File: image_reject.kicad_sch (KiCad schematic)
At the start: 21 parts, among them U1 MXD8546F, U9 MXD8638C

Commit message: Improve power supply filtering and decoupling
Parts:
- C10: value 1uF -> 1 uF
- C31: Substitution (none) -> GRM033R61A105ME44*, GRM033R61C105ME15*, Samsung CL03A105MO3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
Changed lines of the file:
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@@
 			)
 		)
-		(property "Value" "1uF"
+		(property "Value" "1 uF"
 			(at 143.51 171.4499 0)
 			(effects
@@
 			)
 		)
-		(property "Description" ""
+		(property "Description" "CAP CER 1UF 10V X5R 0201"
 			(at 151.13 170.18 0)
 			(effects
@@
 			(at 151.13 170.18 0)
 			(effects
+				(font
+					(size 1.27 1.27)
+				)
+				(hide yes)
+			)
+		)
+		(property "Substitution" "GRM033R61A105ME44*, GRM033R61C105ME15*, Samsung CL03A105MO3NRN*"
+			(at 151.13 170.18 0)
+			(effects

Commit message: Change SP3T RF switches from MXD8638C to BGS13SN8
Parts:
- U9: value MXD8638C -> BGS13SN8; symbol praline:MXD8638 -> praline:BGS13SN8; Manufacturer Maxscend -> Infineon; Part Number MXD8638C -> BGS13SN8E6327XTSA1
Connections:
- net 2V5RF: now also U9.1 (VDD); no longer U9.7 (VDD)
- net GND: now also U9.8 (GND); no longer U9.6 (GND)
- net LPF_OR_MIX_BYPASS: now also U9.2 (V2); no longer U9.8 (V2)
- net MIX_BYPASS: now also U9.7 (RF2); no longer U9.5 (RF2)
- net MIX_EN: now also U9.3 (V1); no longer U9.1 (V1)
- net RF: now also U9.6 (RFin); no longer U9.4 (ANT)
- net at C61.1, L15.1: now also U9.4 (RF3); no longer U9.2 (RF3)
- net at C96.2: now also U9.5 (RF1); no longer U9.3 (RF1)
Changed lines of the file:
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@@
 	)
 	(symbol
-		(lib_id "praline:MXD8638")
+		(lib_id "praline:BGS13SN8")
 		(at 224.79 69.85 0)
 		(unit 1)
@@
 			)
 		)
-		(property "Value" "MXD8638C"
+		(property "Value" "BGS13SN8"
 			(at 204.47 67.31 0)
 			(effects
@@
 			)
 		)
-		(property "Datasheet" "https://www.lcsc.com/datasheet/lcsc_datasheet_1912301210_Maxscend-MXD8638C_C285557.pdf"
+		(property "Datasheet" "https://www.infineon.com/dgdl/Infineon-BGS13SN8-DS-v02_02-EN.pdf?fileId=5546d462584d1d4a0158cf52e3ae03a7"
 			(at 224.79 69.85 0)
 			(effects
@@
 			)
 		)
-		(property "Manufacturer" "Maxscend"
+		(property "Manufacturer" "Infineon"
 			(at 224.79 69.85 0)
 			(effects
@@
 			)
 		)
-		(property "Part Number" "MXD8638C"
+		(property "Part Number" "BGS13SN8E6327XTSA1"
 			(at 224.79 69.85 0)
 			(effects

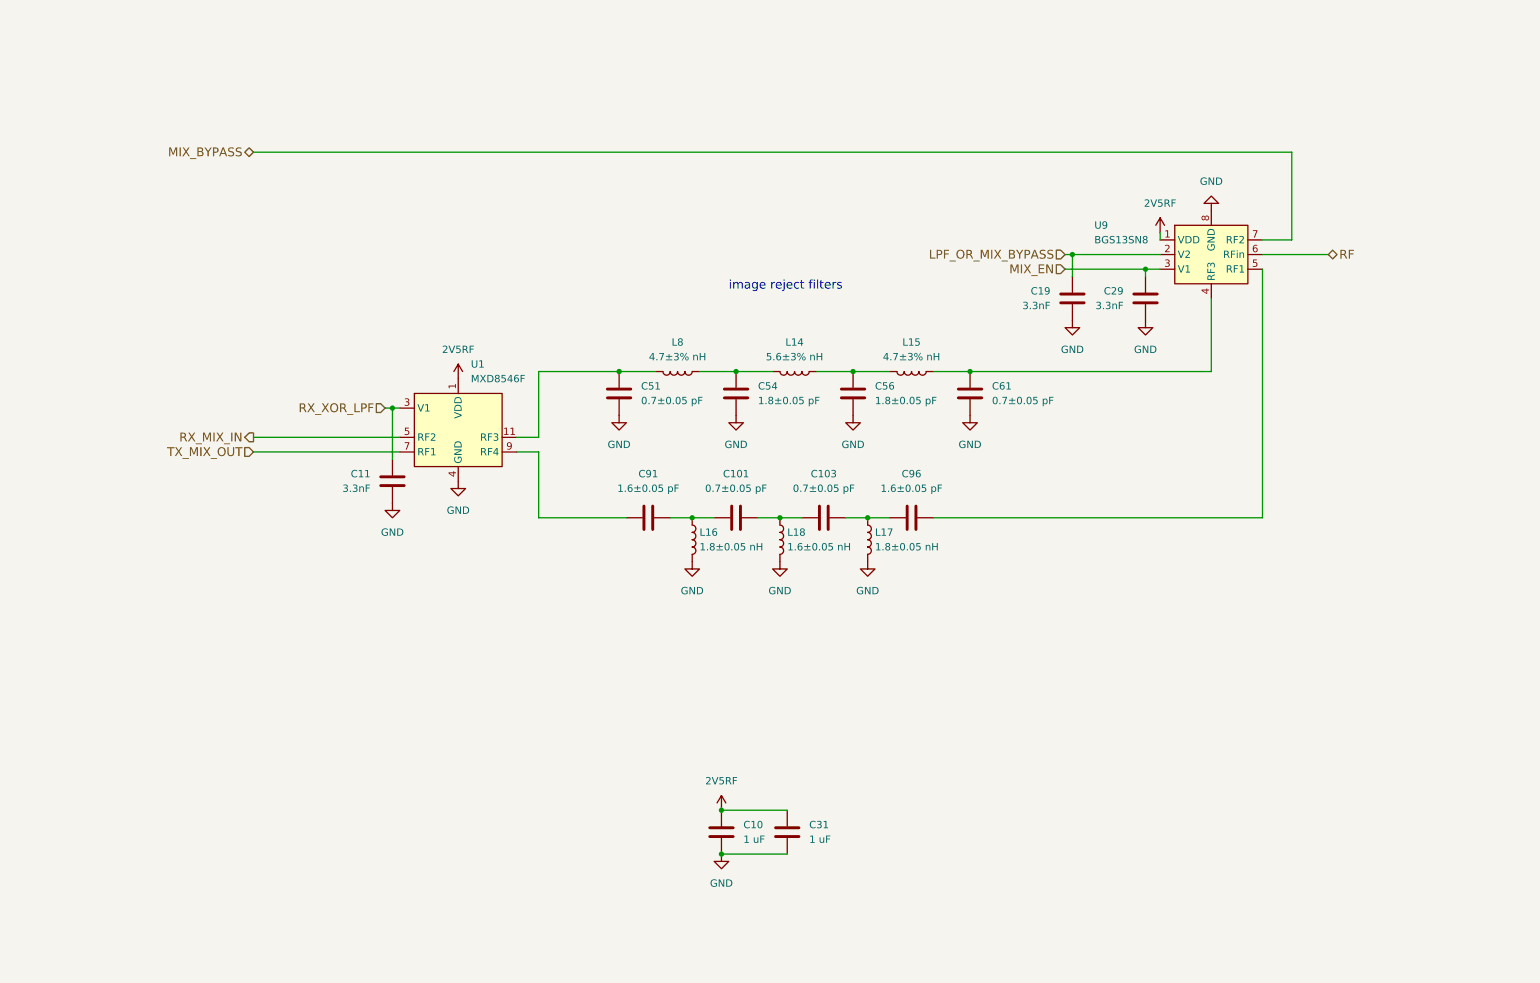
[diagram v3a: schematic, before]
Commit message: Add mixer loss compensation amplifiers
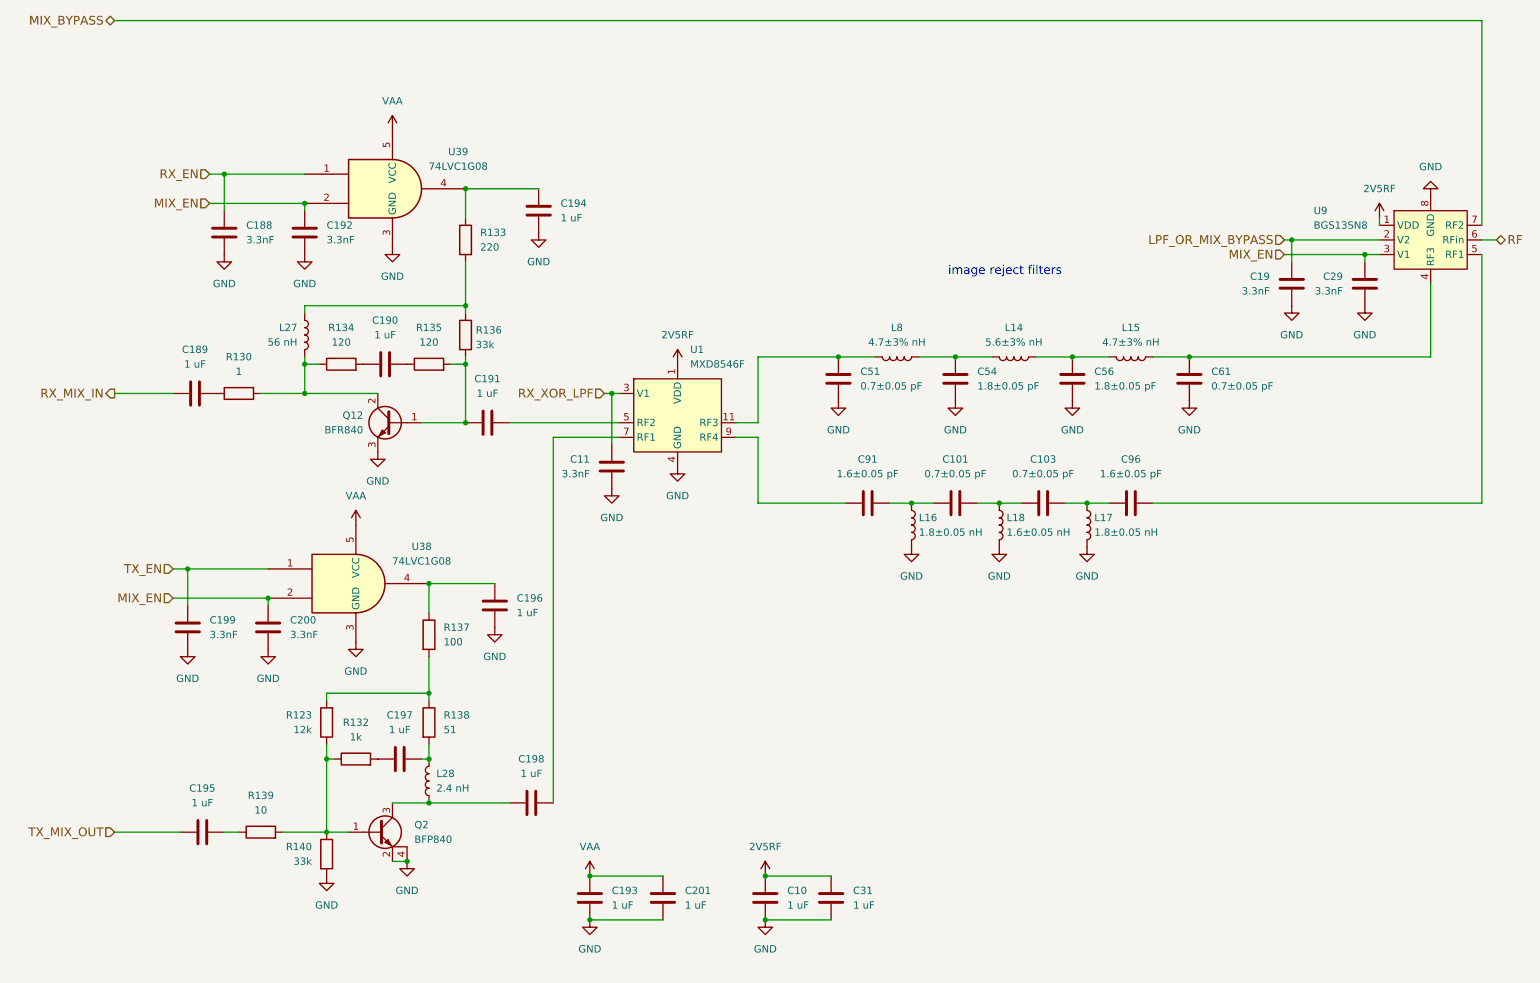
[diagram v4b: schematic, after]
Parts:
- added C188, C192, C199, C200: 3.3nF, Capacitor_SMD:C_0201_0603Metric, symbol Device:C
- added C189, C190, C191, C193, C194, C195, C196, C197, C198, C201: 1 uF, Capacitor_SMD:C_0201_0603Metric, symbol Device:C
- added L27: 56 nH, Inductor_SMD:L_0201_0603Metric, symbol Device:L
- added L28: 2.4 nH, Inductor_SMD:L_0201_0603Metric, symbol Device:L
- added Q12: BFR840, praline:TSLP-3-9, symbol Transistor_BJT:Q_NPN_BCE
- added Q2: BFP840, praline:SOT-343-4-3, symbol praline:Q_NPN_BECE
- added R123: 12k, Resistor_SMD:R_0201_0603Metric, symbol Device:R
- added R130: 1, Resistor_SMD:R_0201_0603Metric, symbol Device:R
- added R132: 1k, Resistor_SMD:R_0201_0603Metric, symbol Device:R
- added R133: 220, Resistor_SMD:R_0201_0603Metric, symbol Device:R
- added R134, R135: 120, Resistor_SMD:R_0201_0603Metric, symbol Device:R
- added R136, R140: 33k, Resistor_SMD:R_0201_0603Metric, symbol Device:R
- added R137: 100, Resistor_SMD:R_0201_0603Metric, symbol Device:R
- added R138: 51, Resistor_SMD:R_0201_0603Metric, symbol Device:R
- added R139: 10, Resistor_SMD:R_0201_0603Metric, symbol Device:R
- added U38, U39: 74LVC1G08, Package_TO_SOT_SMD:SOT-353_SC-70-5, symbol 74xGxx:74LVC1G08
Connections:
- net GND: now also C188.1, C192.1, C193.2, C194.2, C196.2, C199.1, C200.1, C201.2, Q12.3 (E), Q2.2 (E), Q2.4 (C), R140.2, U38.3 (GND), U39.3 (GND)
- net MIX_EN: now also C192.2, C200.2, U38.2, U39.2
- net RX_MIX_IN: now also C189.1; no longer U1.5 (RF2)
- net TX_MIX_OUT: now also C195.2; no longer U1.7 (RF1)
- new net: C190.2, R135.1
- new net: C191.2, Q12.1 (B), R135.2, R136.2
- new net: C190.1, R134.2
- new net: C191.1, U1.5 (RF2)
- new net: C189.2, R130.1
- new net: L27.2, Q12.2 (C), R130.2, R134.1
- new net: Q2.1 (B), R123.1, R132.1, R139.2, R140.1
- new net: C198.2, L28.1, Q2.3 (C)
- new net: C196.1, R137.1, U38.4
- new net: C197.2, R132.2
- new net: C194.1, R133.1, U39.4
- new net: C197.1, L28.2, R138.2
- new net: C198.1, U1.7 (RF1)
- new net: R123.2, R137.2, R138.1
- new net: C195.1, R139.1
- new net: L27.1, R133.2, R136.1
- new net RX_EN: C188.2, U39.1
- new net TX_EN: C199.2, U38.1
- new net VAA: C193.1, C201.1, U38.5 (VCC), U39.5 (VCC)
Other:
- moved on the sheet: C10, C101, C103, C11, C19, C29, C31, C51, C54, C56, C61, C91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

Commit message: Add supply FETs to RF amplifiers
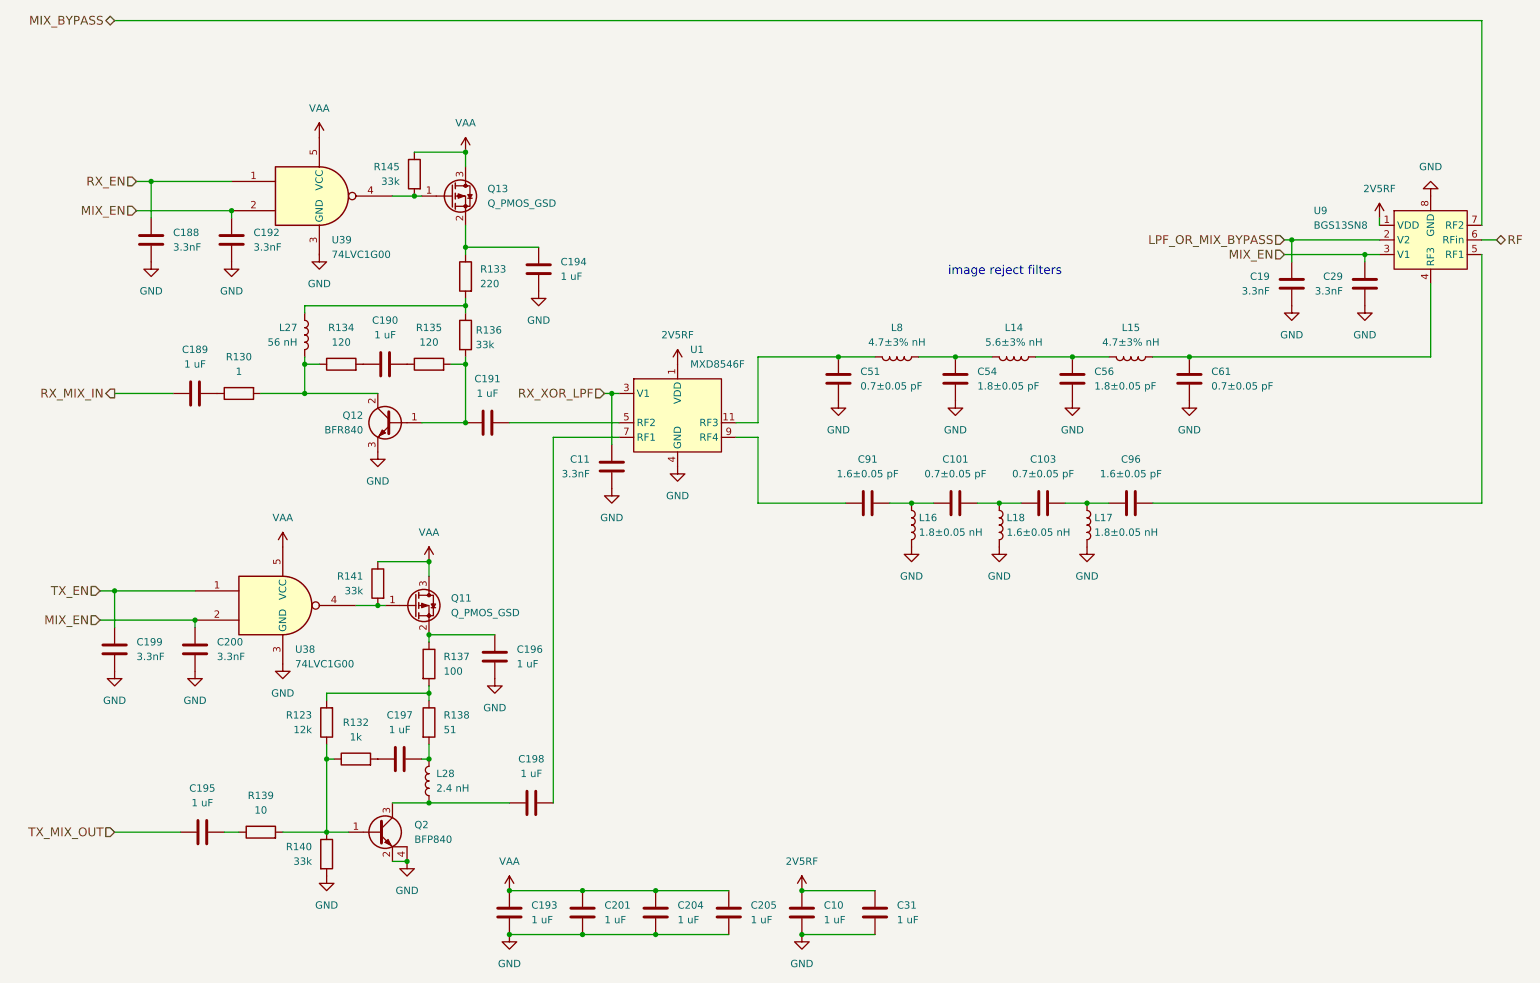
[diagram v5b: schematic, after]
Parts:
- removed U38, U39: 74LVC1G08, Package_TO_SOT_SMD:SOT-353_SC-70-5, symbol 74xGxx:74LVC1G08
- added C204, C205: 1 uF, Capacitor_SMD:C_0201_0603Metric, symbol Device:C
- added Q11, Q13: Q_PMOS_GSD, praline:TSLP-3-9, symbol Transistor_FET:Q_PMOS_GSD
- added R141, R145: 33k, Resistor_SMD:R_0201_0603Metric, symbol Device:R
- added U38, U39: 74LVC1G00, Package_TO_SOT_SMD:SOT-353_SC-70-5, symbol 74xGxx:74LVC1G00
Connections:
- net GND: now also C204.2, C205.2, U38.3 (GND), U39.3 (GND)
- net MIX_EN: now also U38.2, U39.2
- net RX_EN: now also U39.1
- net TX_EN: now also U38.1
- net VAA: now also C204.1, C205.1, Q11.3 (D), Q13.3 (D), R141.1, R145.1, U38.5 (VCC), U39.5 (VCC)
- net at C196.1, R137.1: now also Q11.2 (S)
- net at C194.1, R133.1: now also Q13.2 (S)
- new net: Q13.1 (G), R145.2, U39.4
- new net: Q11.1 (G), R141.2, U38.4
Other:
- moved on the sheet: C10, C188, C192, C193, C194, C196, C199, C200, C201, C31, R133, R137

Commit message: Use consistent footprints for 0402 and 0201 diodes
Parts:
- Q11, Q13: Manufacturer NRC -> LRC
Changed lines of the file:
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@@
 			)
 		)
-		(property "Manufacturer" "NRC"
+		(property "Manufacturer" "LRC"
 			(at 92.71 59.69 0)
 			(effects
@@
 			)
 		)
-		(property "Manufacturer" "NRC"
+		(property "Manufacturer" "LRC"
 			(at 86.36 130.81 0)
 			(effects
